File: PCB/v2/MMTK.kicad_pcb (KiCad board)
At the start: 4 copper layers, 135.5 x 60 mm, 100 parts, among them J2 Stepper, J3 LoadCell, J4 Barrel_Jack_Switch, J5 LCD, J7 ESTOP_SOFT, Q1 MMBT4403LT1G, Q2 Q_PMOS_GSD, Q3 2N7002, Q4 2N7002, Q5 2N7002, U1 HX711, U2 TMC2209, U3 TPS562200

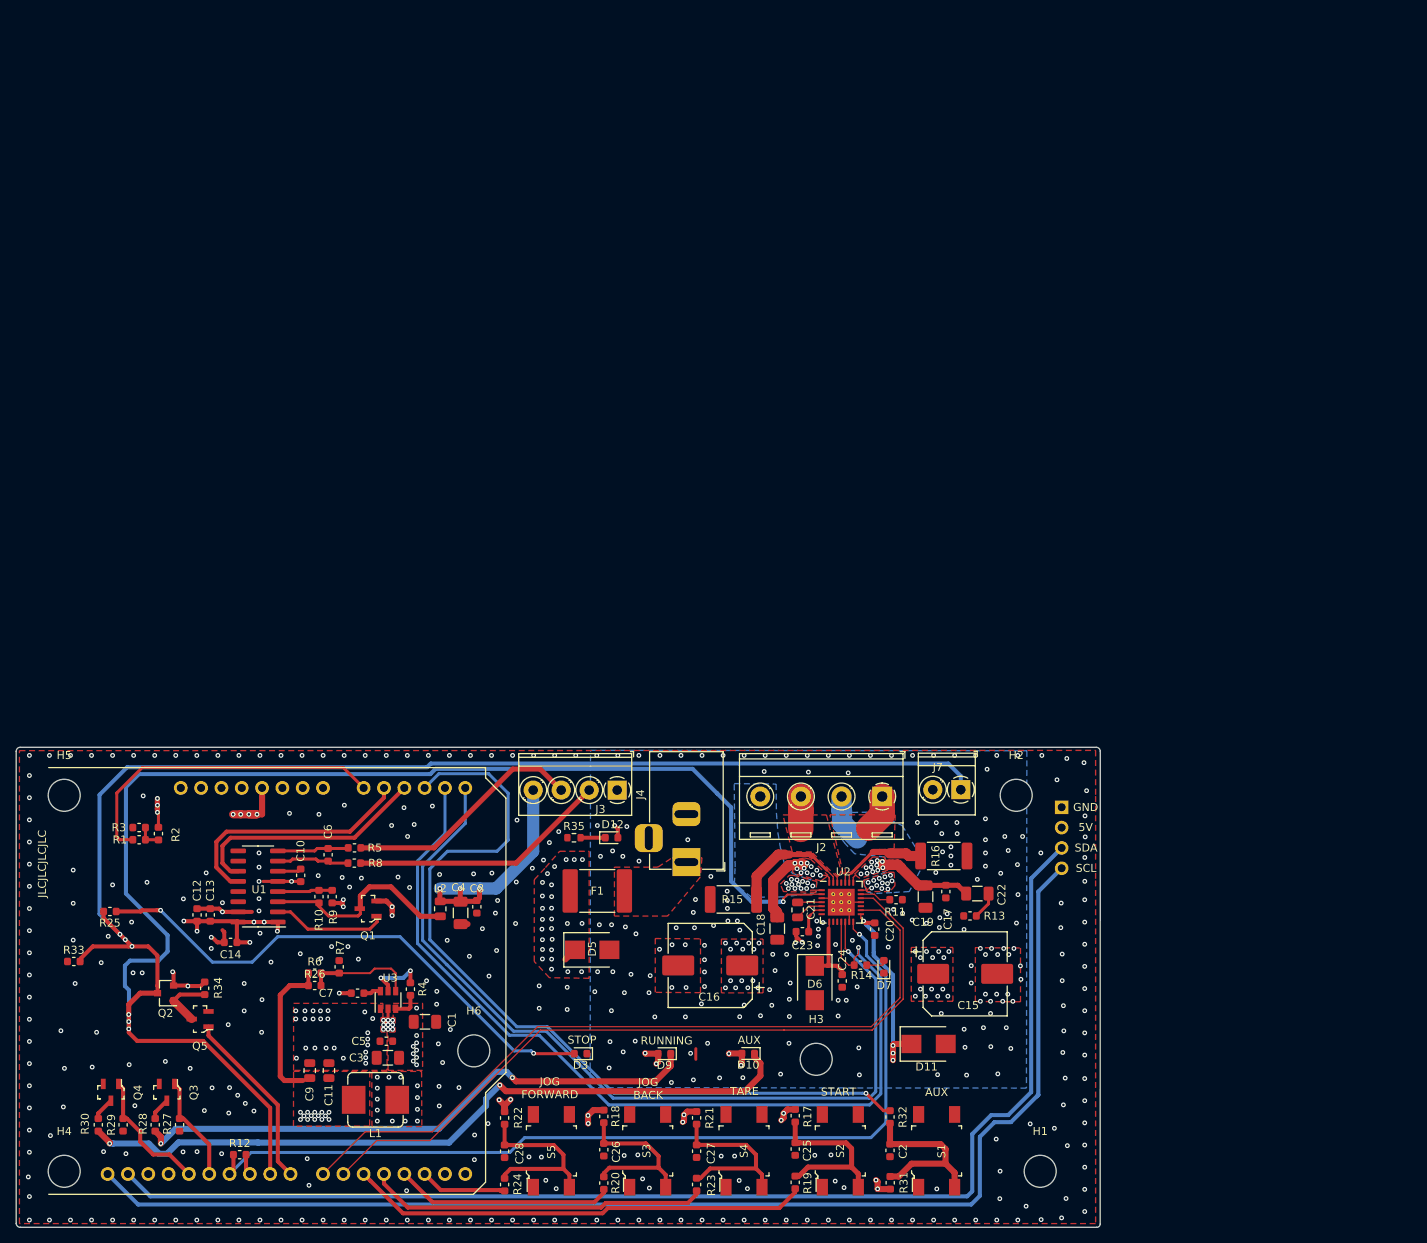
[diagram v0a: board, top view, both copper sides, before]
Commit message: Tore up PCB
Tore up PCB, just need to reroute whole thing easier than trying to reuse existing.
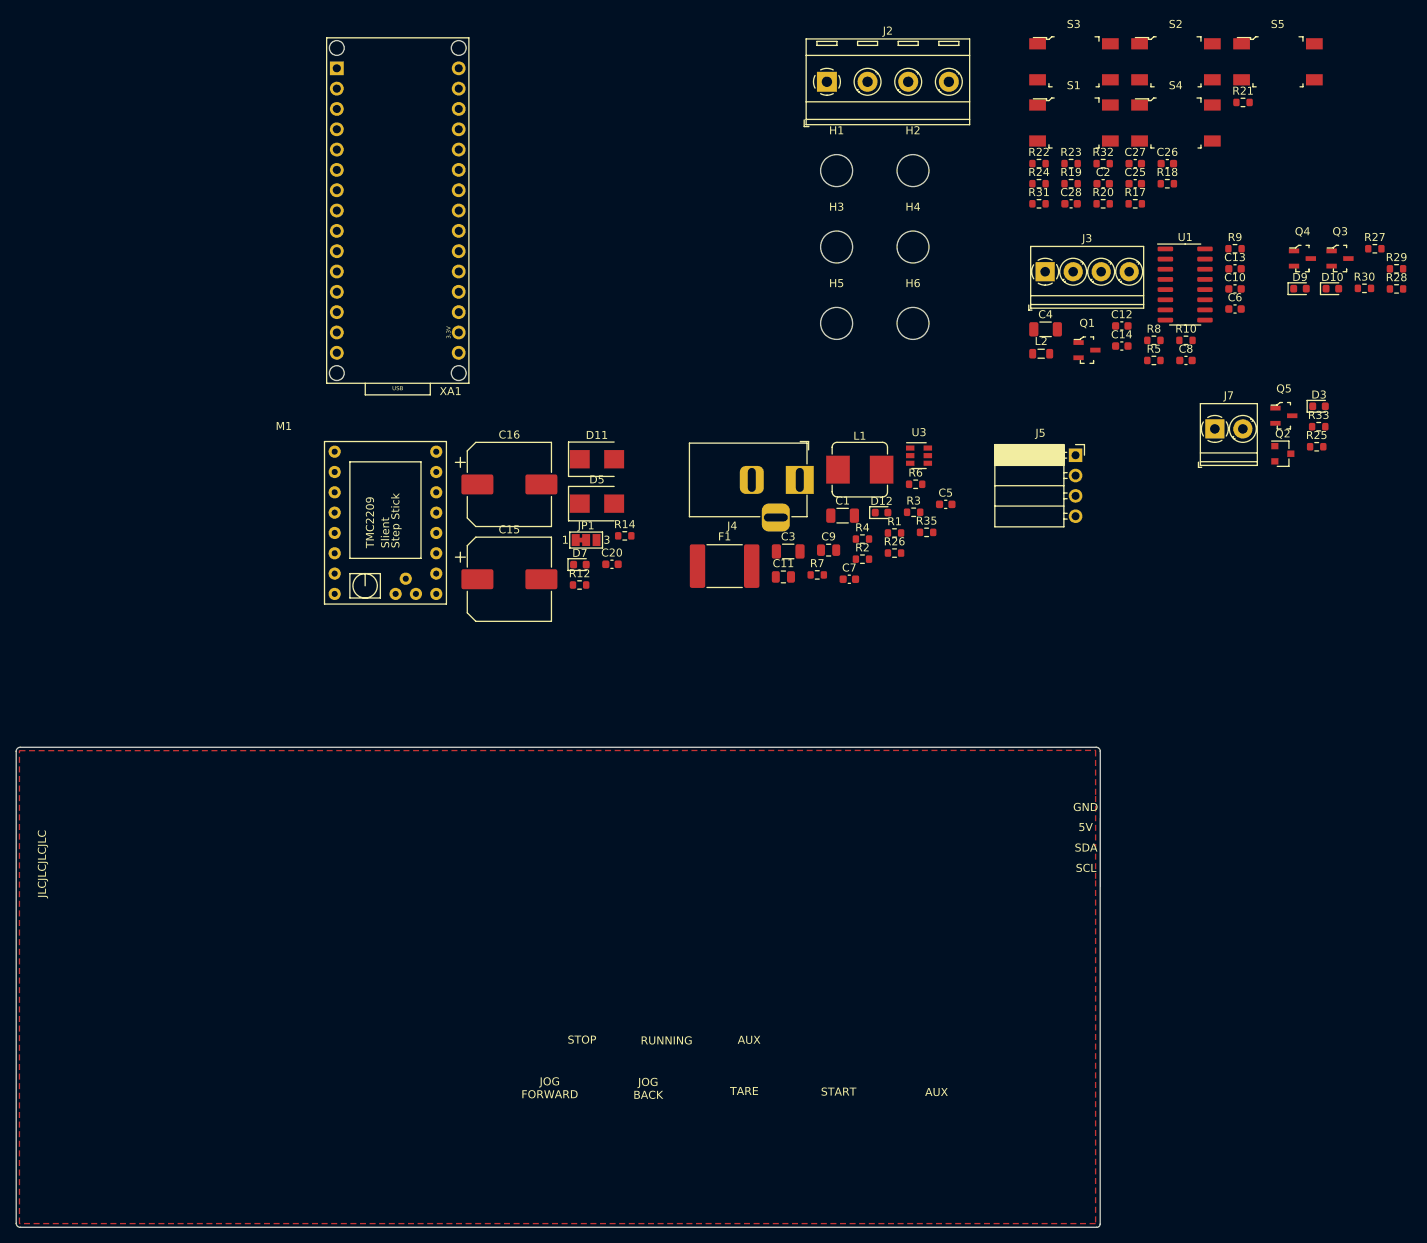
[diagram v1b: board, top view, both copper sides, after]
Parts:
- removed C17, C23: 100n, Capacitor_SMD:C_0603_1608Metric
- removed C18, C19: 10u, Capacitor_SMD:C_1206_3216Metric
- removed C21: 22n, Capacitor_SMD:C_0805_2012Metric
- removed C22: 1u, Capacitor_SMD:C_1206_3216Metric
- removed C24: 2u2, Capacitor_SMD:C_0603_1608Metric
- removed D6: SMBJ5A, Diode_SMD:D_SMB
- removed R11: 100k/1%, Resistor_SMD:R_0603_1608Metric
- removed R13: 1R/1%, Resistor_SMD:R_0603_1608Metric
- removed R15, R16: 100mR/1W, Resistor_SMD:R_2512_6332Metric
- removed R34: 20K, Resistor_SMD:R_0603_1608Metric
- removed U2: TMC2209, Package_DFN_QFN:QFN-28-1EP_5x5mm_P0.5mm_EP3.35x3.35mm_ThermalVias
- added JP1: Jumper_3_Bridged12, Jumper:SolderJumper-3_P1.3mm_Bridged12_Pad1.0x1.5mm_NumberLabels, F.Cu at (71.2, -25.9)
- added M1: TMC2209-Module, MMTK:TMCC2209_Module, F.Cu at (39.8, -37.0)
- J5: moved to F.Cu
- XA1: value Arduino_Uno_Shield_NoICSP -> Arduino_Nano_Socket; footprint MMTK:Arduino_Uno_Shield_NoICSP -> Arduino:Arduino_Nano_Socket; moved to F.Cu
- moved R29 191.8 mm to (172.5, -59.8), turned to 0 degrees
- moved R30 189.7 mm to (168.5, -57.4), turned to 0 degrees
- moved R28 187.1 mm to (172.5, -57.3), turned to 0 degrees
- moved R27 185.2 mm to (169.8, -62.3), turned to 0 degrees
- moved Q4 181.8 mm to (160.8, -61.1), turned to 0 degrees
- moved Q3 179.9 mm to (165.5, -61.1), turned to 0 degrees
- moved R33 169.4 mm to (162.8, -40.1)
- moved S5 163.7 mm to (157.7, -85.7), turned to 0 degrees
- moved R25 161.6 mm to (162.6, -37.6), turned to 0 degrees
- moved H4 156.9 mm to (112.1, -62.5)
- moved Q2 155.1 mm to (158.3, -36.7), turned to 0 degrees
- moved Q5 155.0 mm to (158.5, -41.4), turned to 0 degrees
- moved C13 151.4 mm to (152.4, -59.8), turned to 0 degrees
- moved S3 146.2 mm to (132.2, -85.7), turned to 0 degrees
- moved R21 144.1 mm to (153.4, -80.6), turned to 0 degrees
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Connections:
- J7 pad 1: /SERVO_ENN -> Net-(J7-Pad1)
- J7 pad 2: +5V -> /SERVO_ENN
- Q2 pad 1: Net-(Q2-Pad1) -> /SERVO_ENN
- Q2 pad 3: /SERVO_ENN -> Net-(Q2-Pad3)
- Q5 pad 3: Net-(Q2-Pad1) -> Net-(J7-Pad1)
- R25 pad 2: /SERVO_ENN -> Net-(Q2-Pad3)
- R33 pad 1: GND -> /SERVO_ENN
- R33 pad 2: /SERVO_ENN -> +5V
- XA1 pad A4: /SERVO_DIAG -> /LCD_SDA
- XA1 pad A5: /SERVO_INDEX -> /LCD_SCL
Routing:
- net /SERVO_ENN: track 329.6 -> 0.00 mm, vias 7 -> 0
- net /LCD_SCL: track 157.5 -> 0.00 mm
- net /LCD_SDA: track 155.7 -> 0.00 mm
- net +5V: track 119.1 -> 0.00 mm, vias 47 -> 0
- net /SERVO_DIAG: track 116.2 -> 0.00 mm, vias 1 -> 0
- net /SERVO_UART_RX: track 114.2 -> 0.00 mm, vias 1 -> 0
- net /SERVO_INDEX: track 109.6 -> 0.00 mm, vias 1 -> 0
- net /BT4: track 104.6 -> 0.00 mm, vias 1 -> 0
- net /SERVO_STEP: track 95.7 -> 0.00 mm
- net /SERVO_DIR: track 94.7 -> 0.00 mm
- net Net-(D10-Pad1): track 92.3 -> 0.00 mm, vias 2 -> 0
- net +12V: track 88.7 -> 0.00 mm, vias 90 -> 0
- net Net-(D9-Pad1): track 72.1 -> 0.00 mm, vias 2 -> 0
- net Net-(D3-Pad2): track 67.4 -> 0.00 mm, vias 2 -> 0
- net /BT0: track 57.5 -> 0.00 mm
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- removed copper zone on F.Cu, net +12V
- removed copper zone on In2.Cu, net +12V
- removed copper zone on F.Cu, net +5V
- removed copper zone on F.Cu, net /TMC2209/OA1
- removed copper zone on B.Cu, net /TMC2209/OA2
- removed copper zone on F.Cu, net /TMC2209/OA2
- removed copper zone on F.Cu, net /TMC2209/OB1
- removed copper zone on B.Cu, net /TMC2209/OB2
- removed copper zone on F.Cu, net /TMC2209/OB2
- removed copper zone on B.Cu, net GND
- removed copper zone on F.Cu, net Net-(C7-Pad1)
- removed copper zone on In2.Cu, net Net-(C7-Pad1)
- removed copper zone on F.Cu, net Net-(F1-Pad1)
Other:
- board text removed: "MMTK V1.0"

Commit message: WIP updated symbols for tmc5106
Updated footprint for tmc5106,
need to check how motor wiring is done, might be wired up stupid before and that's gonna be sad
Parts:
- removed M1: TMC2209-Module, MMTK:TMCC2209_Module
- added JP2: Jumper_3_Bridged12, Jumper:SolderJumper-3_P1.3mm_Bridged12_Pad1.0x1.5mm_NumberLabels, F.Cu at (-27.6, -74.2)
- added JP3: Jumper_3_Bridged12, Jumper:SolderJumper-3_P1.3mm_Bridged12_Pad1.0x1.5mm_NumberLabels, F.Cu at (-14.2, -77.2)
- added JP4: Jumper_3_Bridged12, Jumper:SolderJumper-3_P1.3mm_Bridged12_Pad1.0x1.5mm_NumberLabels, F.Cu at (-33.3, -74.2)
- added JP5: Jumper_3_Bridged12, Jumper:SolderJumper-3_P1.3mm_Bridged12_Pad1.0x1.5mm_NumberLabels, F.Cu at (-22.0, -74.2)
- added JP6: Jumper_3_Bridged12, Jumper:SolderJumper-3_P1.3mm_Bridged12_Pad1.0x1.5mm_NumberLabels, F.Cu at (-33.3, -44.3)
- added Q6: 2N7002, digikey-footprints:SOT-23-3, F.Cu at (-28.7, -141.1)
- added R11: 110K, Resistor_SMD:R_0603_1608Metric, F.Cu at (41.4, -80.3)
- added R13: 20K, Resistor_SMD:R_0603_1608Metric, F.Cu at (9.27, -32.3)
- added R15: 300K, Resistor_SMD:R_0603_1608Metric, F.Cu at (5.11, -27.7)
- added U2: TMC5160_Module, MMTK:TMCC2209_Module_copy, F.Cu at (115.6, 14.0)
- R12: value 1k/1% -> 20K
- R3: value 100K/1% -> 1k/1%
- moved S5 235.7 mm to (-74.7, -124.5)
- moved S2 226.3 mm to (-74.7, -139.8)
- moved S4 226.3 mm to (-74.7, -132.1)
- moved Q1 222.2 mm to (-78.7, -114.3)
- moved Q5 216.2 mm to (-33.4, -141.1)
- moved Q3 210.9 mm to (-33.4, -131.5)
- moved Q4 202.1 mm to (-28.7, -131.5)
- moved S1 201.6 mm to (-62.0, -132.1)
- moved S3 201.6 mm to (-62.0, -139.8)
- moved R10 182.3 mm to (-34.1, -24.4)
- moved C10 178.7 mm to (-23.9, -27.7)
- moved C8 174.1 mm to (-26.1, -23.2)
- moved C6 172.9 mm to (-18.1, -25.9)
- moved C12 170.9 mm to (-30.1, -23.2)
- moved R8 166.7 mm to (-22.1, -22.7)
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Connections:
- J2 pad 1: /TMC2209/OA1 -> /TMC_SlientStepStick/OA1
- J2 pad 2: /TMC2209/OA2 -> /TMC_SlientStepStick/OA2
- J2 pad 3: /TMC2209/OB1 -> /TMC_SlientStepStick/OB1
- J2 pad 4: /TMC2209/OB2 -> /TMC_SlientStepStick/OB2
- JP1 pad 3: Net-(JP1-Pad3) -> /TMC_SDI
- Q5 pad 2: GND -> Net-(Q5-Pad2)
- R12 pad 1: /SERVO_UART_RX -> +12V
- R12 pad 2: /SERVO_UART_TX -> Net-(Q6-Pad1)
- R14 pad 2: /SERVO_DIAG -> Net-(JP6-Pad2)
- R3 pad 1: GND -> Net-(JP1-Pad1)
- R3 pad 2: Net-(R1-Pad2) -> Net-(JP3-Pad1)
- S1 pad 1: (no net) -> unconnected-(S1-Pad1)
- S1 pad 4: (no net) -> unconnected-(S1-Pad4)
- S2 pad 1: (no net) -> unconnected-(S2-Pad1)
- S2 pad 4: (no net) -> unconnected-(S2-Pad4)
- S3 pad 1: (no net) -> unconnected-(S3-Pad1)
- S3 pad 4: (no net) -> unconnected-(S3-Pad4)
- S4 pad 1: (no net) -> unconnected-(S4-Pad1)
- S4 pad 4: (no net) -> unconnected-(S4-Pad4)
- S5 pad 1: (no net) -> unconnected-(S5-Pad1)
- S5 pad 4: (no net) -> unconnected-(S5-Pad4)
- U1 pad 10: (no net) -> unconnected-(U1-Pad10)
- U1 pad 13: (no net) -> unconnected-(U1-Pad13)
- U1 pad 9: (no net) -> unconnected-(U1-Pad9)
- XA1 pad 3V3: (no net) -> unconnected-(XA1-Pad3V3)
- XA1 pad AREF: (no net) -> unconnected-(XA1-PadAREF)
- XA1 pad D0: (no net) -> unconnected-(XA1-PadD0)
- XA1 pad D1: (no net) -> unconnected-(XA1-PadD1)
- XA1 pad D12: /LED0 -> /SERVO_DIR
- XA1 pad D13: /LED1 -> /SERVO_STEP
- XA1 pad D6: /SERVO_DIR -> /LED0
- XA1 pad D7: /SERVO_STEP -> /LED1
- XA1 pad RST1: (no net) -> unconnected-(XA1-PadRST1)
- XA1 pad RST2: (no net) -> unconnected-(XA1-PadRST2)
- XA1 pad VIN: (no net) -> unconnected-(XA1-PadVIN)
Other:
- net class Default removed

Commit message: Updating PCB now
updating pcb now, schematic is done now. Mostly just PCB now
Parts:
- J5: moved to B.Cu
- moved Q1 263.4 mm to (77.5, 97.8)
- moved S1 263.4 mm to (94.2, 80.0)
- moved S2 263.4 mm to (81.5, 72.3)
- moved S3 263.4 mm to (94.2, 72.3)
- moved S4 263.4 mm to (81.5, 80.0)
- moved S5 263.4 mm to (81.5, 87.6)
- moved R12 140.6 mm to (149.9, -38.1)
- moved R13 140.6 mm to (149.9, -35.6)
- moved D3 140.6 mm to (149.9, -40.6)
- moved J7 140.6 mm to (141.6, -37.8)
- moved Q2 140.6 mm to (141.2, -30.0)
- moved R15 140.6 mm to (145.7, -31.0)
- moved R25 140.6 mm to (140.8, -26.6)
- moved R33 140.6 mm to (153.9, -40.7)
- moved J5 114.5 mm to (130.2, 7.58), turned to 180 degrees
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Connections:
- net /TMC_UART0 renamed /TMC_SDO
- net /TMC_UART1 renamed /TMC_SCK
- J2 pad 1: /TMC_SlientStepStick/OA1 -> /TMC_SlientStepStick/OA2
- J2 pad 2: /TMC_SlientStepStick/OA2 -> /TMC_SlientStepStick/OA1
- U2 pad 3: /TMC_SlientStepStick/OB1 -> /TMC_SlientStepStick/OB2
- U2 pad 4: /TMC_SlientStepStick/OA1 -> /TMC_SlientStepStick/OB1
- U2 pad 5: /TMC_SlientStepStick/OA2 -> /TMC_SlientStepStick/OA1
- U2 pad 6: /TMC_SlientStepStick/OB2 -> /TMC_SlientStepStick/OA2

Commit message: Update PCB, sync with git
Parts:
- moved Q5 234.3 mm to (49.0, 78.2), turned to -90 degrees
- moved Q6 226.5 mm to (37.6, 75.4), turned to 180 degrees
- moved C28 208.7 mm to (-36.9, 85.5)
- moved H1 208.0 mm to (128.0, 53.0)
- moved Q4 199.4 mm to (52.1, 50.8), turned to -90 degrees
- moved Q3 198.7 mm to (45.7, 50.8), turned to -90 degrees
- moved R19 197.5 mm to (-53.8, 66.8)
- moved C25 195.5 mm to (-53.8, 69.6)
- moved R17 193.3 mm to (-54.1, 64.3)
- moved D12 192.0 mm to (-57.4, 76.4)
- moved R23 192.0 mm to (-37.4, 68.2)
- moved R35 192.0 mm to (-55.8, 81.4)
- moved C2 192.0 mm to (-45.4, 80.7)
- moved C26 192.0 mm to (-41.4, 73.2)
- moved C27 192.0 mm to (-41.4, 70.7)
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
